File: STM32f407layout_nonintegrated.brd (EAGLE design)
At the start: 61.4 x 71.6 mm, 45 parts, among them Q1 ASF, T3 FDN340P, T4 AP1117_LIN_REG

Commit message: Fixed some wrong info
fixed some stuff
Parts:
- R11, R12, R13, R14: value 83 -> 200
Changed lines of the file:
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@@
 <element name="R1" library="SparkFun-Passives" package="0603-RES" value="10k" x="30.24184375" y="42.22893125" rot="R270"/>
 <element name="R10" library="SparkFun-Passives" package="0603-RES" value="4.7K" x="63.43028125" y="24.979421875" rot="MR180"/>
-<element name="R11" library="SparkFun-Passives" package="0603-RES" value="83" x="28.542509375" y="66.211884375"/>
-<element name="R12" library="SparkFun-Passives" package="0603-RES" value="83" x="28.55059375" y="64.156609375"/>
-<element name="R13" library="SparkFun-Passives" package="0603-RES" value="83" x="28.552184375" y="62.11506875"/>
-<element name="R14" library="SparkFun-Passives" package="0603-RES" value="83" x="28.53085" y="60.0696"/>
+<element name="R11" library="SparkFun-Passives" package="0603-RES" value="200" x="28.542509375" y="66.211884375"/>
+<element name="R12" library="SparkFun-Passives" package="0603-RES" value="200" x="28.55059375" y="64.156609375"/>
+<element name="R13" library="SparkFun-Passives" package="0603-RES" value="200" x="28.552184375" y="62.11506875"/>
+<element name="R14" library="SparkFun-Passives" package="0603-RES" value="200" x="28.53085" y="60.0696"/>
 <element name="R2" library="SparkFun-Passives" package="0603-RES" value="10k" x="30.16184375" y="51.705484375" rot="R90"/>
 <element name="R3" library="SparkFun-Passives" package="0603-RES" value="4.7K" x="35.827084375" y="17.299571875" rot="MR180"/>

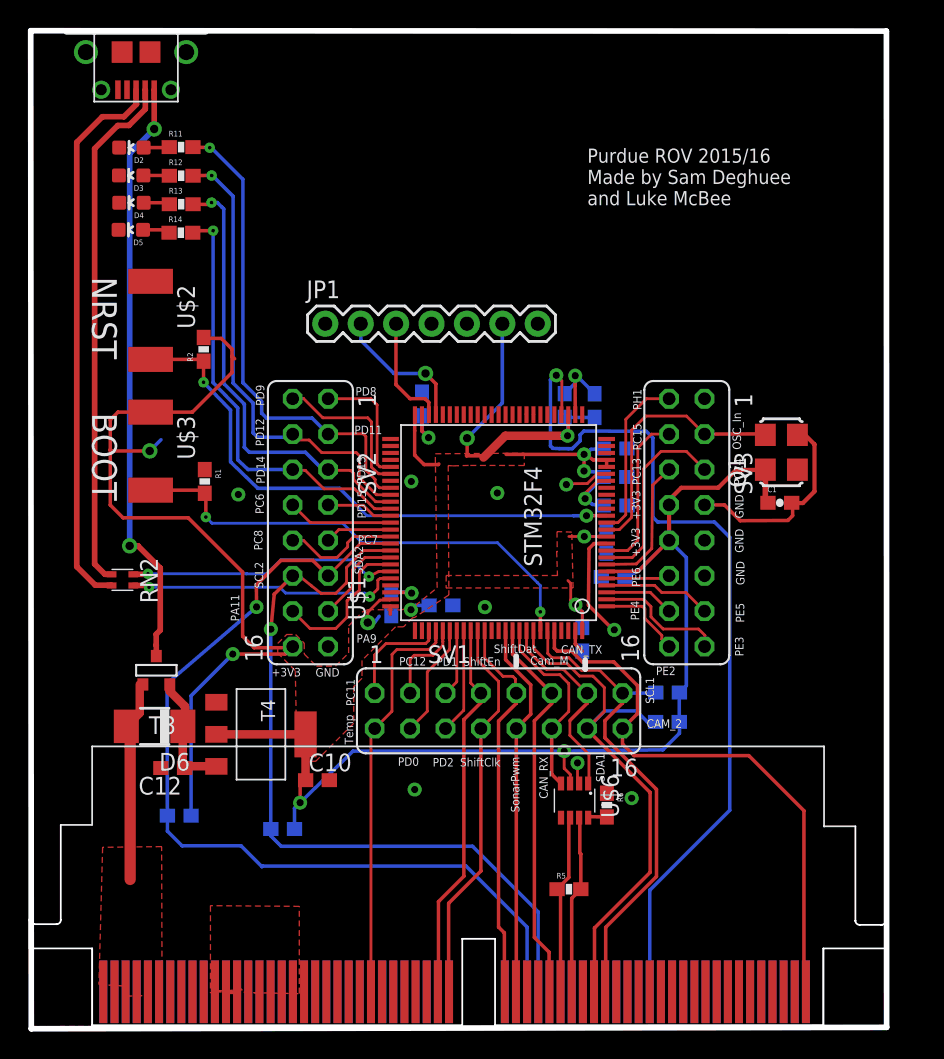
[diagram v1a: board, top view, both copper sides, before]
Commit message: Revision 2.0
Moved LED array, fixed pinout problems
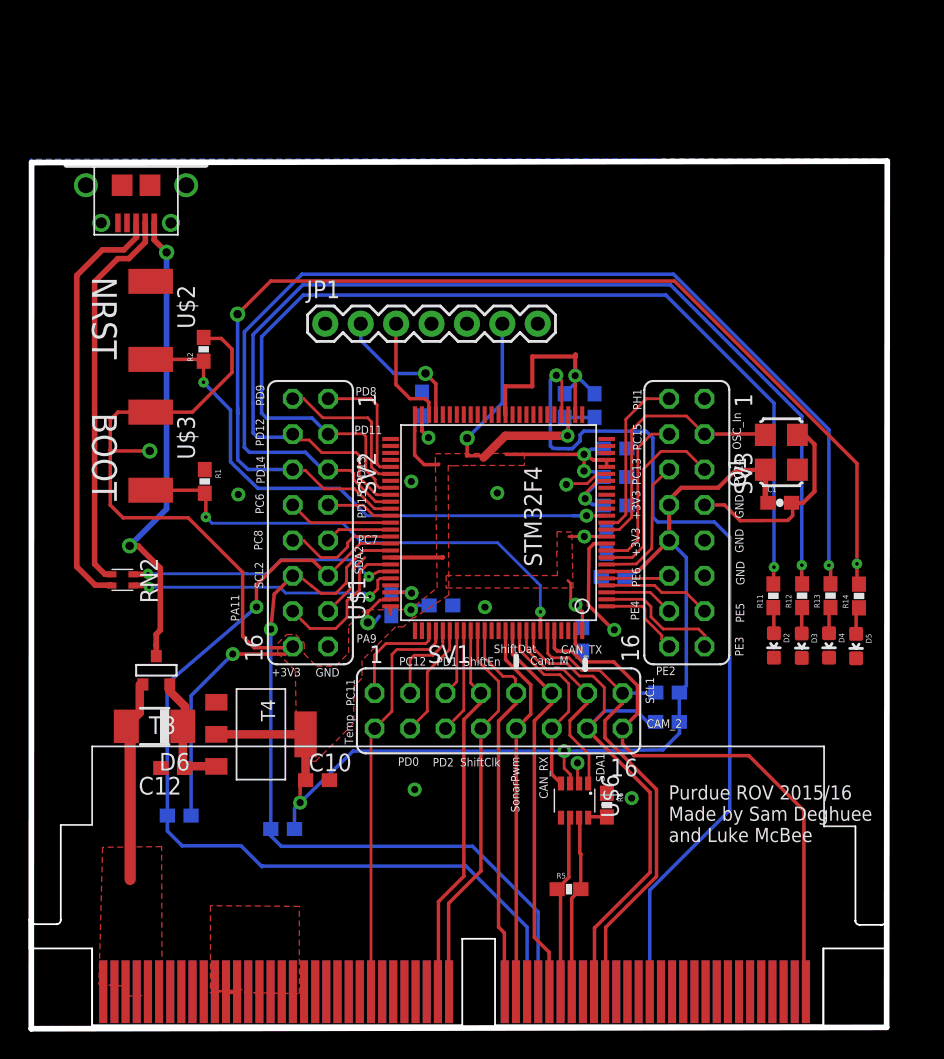
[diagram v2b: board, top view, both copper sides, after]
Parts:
- moved D5 60.0 mm to (77.0, 30.4), turned to 180 degrees
- moved D4 59.3 mm to (75.0, 30.5), turned to 180 degrees
- moved D3 58.7 mm to (73.1, 30.4), turned to 180 degrees
- moved D2 58.3 mm to (71.1, 30.5), turned to 180 degrees
- moved R14 55.2 mm to (77.2, 34.0), turned to 90 degrees
- moved R13 54.4 mm to (75.1, 34.0), turned to 90 degrees
- moved R12 53.8 mm to (73.1, 34.0), turned to 90 degrees
- moved R11 53.3 mm to (71.0, 34.0), turned to 90 degrees
- moved U$5 9.55 mm to (25.3, 64.9)
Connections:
- removed net PB2: U$1.P37
- net +3V3: now also U$1.P68
- net GND: now also U$1.P37
- net PA9: no longer U$1.P68
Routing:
- net PD14: track 31.1 -> 82.8 mm, vias 1 -> 2
- net PD13: track 32.6 -> 80.1 mm
- net PD12: track 33.9 -> 76.7 mm
- net PD11: track 34.9 -> 72.8 mm
- net GND: track 41.6 -> 52.6 mm
- net N$12: track 37.5 -> 28.0 mm
- net N$24: track 40.0 -> 30.4 mm
- net N$57: track 42.7 -> 33.9 mm
- net +3V3: track 203.4 -> 205.7 mm
- net PA9: track 6.79 -> 4.94 mm
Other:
- board size 61.4 x 71.6 mm -> 61.4 x 62.2 mm

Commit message: Fixed PA9 and routed
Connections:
- removed net N$57: T3.1, U$5.P1
- removed net PA9: SV2.13
- new net USBPWR: SV2.13, T3.1, U$1.P68, U$5.P1
- net +3V3: no longer U$1.P68
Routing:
- net USBPWR: track 0.00 -> 58.9 mm, vias 0 -> 3
- net N$57: track 33.9 -> 0.00 mm, vias 2 -> 0
- net PA9: track 4.94 -> 0.00 mm
- net +3V3: track 205.7 -> 202.0 mm
- net I2C3_SDA: track 65.7 -> 66.6 mm, vias 1 -> 3
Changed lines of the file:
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@@
 <wire x1="49.017896875" y1="44.068009375" x2="50.108815625" y2="44.068009375" width="0.254" layer="1"/>
 <wire x1="50.108815625" y1="44.068009375" x2="50.23609375" y2="43.94073125" width="0.254" layer="1"/>
-<contactref element="U$1" pad="P68"/>
-<wire x1="43.56884375" y1="36.773040625" x2="47.318434375" y2="36.773040625" width="0.3048" layer="1"/>
-<wire x1="47.318434375" y1="36.773040625" x2="47.318434375" y2="36.805353125" width="0.3048" layer="1"/>
 </signal>
 <signal name="N$3">
@@
 <contactref element="R3" pad="1"/>
 <contactref element="SV2" pad="12"/>
-<wire x1="43.56884375" y1="37.273040625" x2="41.62684375" y2="37.273040625" width="0.2032" layer="1"/>
-<wire x1="41.62684375" y1="37.273040625" x2="40.41184375" y2="36.058040625" width="0.2032" layer="1"/>
-<wire x1="40.41184375" y1="36.058040625" x2="40.41184375" y2="34.961040625" width="0.2032" layer="1"/>
 <wire x1="40.41184375" y1="34.961040625" x2="40.39584375" y2="34.945040625" width="0.2032" layer="1"/>
 <wire x1="40.39584375" y1="34.945040625" x2="40.38084375" y2="34.945040625" width="0.2032" layer="1"/>
@@
 <wire x1="34.977084375" y1="31.899290625" x2="34.983928125" y2="31.629703125" width="0.254" layer="16"/>
 <via x="34.983928125" y="31.629703125" extent="1-16" drill="0.508"/>
-<wire x1="34.983928125" y1="31.629703125" x2="35.2258375" y2="34.140034375" width="0.254" layer="1"/>
-<wire x1="35.2258375" y1="34.140034375" x2="36.54884375" y2="35.463040625" width="0.254" layer="1"/>
 <wire x1="34.977084375" y1="17.299571875" x2="34.977084375" y2="16.8021875" width="0.254" layer="16"/>
 <wire x1="34.977084375" y1="16.8021875" x2="35.72144375" y2="16.057828125" width="0.254" layer="16"/>
@@
 <wire x1="54.1567125" y1="11.353521875" x2="54.1567125" y2="5.628225" width="0.254" layer="16"/>
 <wire x1="54.1567125" y1="5.628225" x2="54.163659375" y2="5.621278125" width="0.254" layer="16"/>
+<wire x1="40.41184375" y1="34.961040625" x2="40.41184375" y2="36.22315" width="0.2032" layer="1"/>
+<wire x1="40.41184375" y1="36.22315" x2="41.456471875" y2="37.267778125" width="0.2032" layer="1"/>
+<wire x1="41.456471875" y1="37.267778125" x2="43.56358125" y2="37.267778125" width="0.2032" layer="1"/>
+<wire x1="43.56358125" y1="37.267778125" x2="43.56884375" y2="37.273040625" width="0.2032" layer="1"/>
+<wire x1="36.54884375" y1="35.463040625" x2="34.983928125" y2="33.898125" width="0.2032" layer="1"/>
+<wire x1="34.983928125" y1="33.898125" x2="34.983928125" y2="31.629703125" width="0.2032" layer="1"/>
 </signal>
 <signal name="I2C3_SDA">
@@
 <wire x1="41.39884375" y1="37.773040625" x2="39.08884375" y2="35.463040625" width="0.2032" layer="1"/>
 <wire x1="27.561375" y1="18.2559375" x2="27.539353125" y2="27.739171875" width="0.254" layer="16"/>
-<wire x1="27.539353125" y1="27.739171875" x2="33.954415625" y2="33.223175" width="0.254" layer="16"/>
 <via x="33.954415625" y="33.223175" extent="1-16" drill="0.508"/>
 <wire x1="33.954415625" y1="33.223175" x2="33.94585625" y2="34.804046875" width="0.254" layer="1"/>
@@
 <wire x1="48.98438125" y1="14.63629375" x2="34.38481875" y2="14.63629375" width="0.254" layer="16"/>
 <wire x1="34.38481875" y1="14.63629375" x2="34.343415625" y2="14.594890625" width="0.254" layer="16"/>
+<via x="31.108665625" y="31.83608125" extent="1-16" drill="0.6"/>
+<wire x1="31.108665625" y1="31.83608125" x2="29.4826375" y2="29.419990625" width="0.2032" layer="1"/>
+<wire x1="29.4826375" y1="29.419990625" x2="29.4826375" y2="28.851025" width="0.2032" layer="1"/>
+<via x="29.4826375" y="28.851025" extent="1-16" drill="0.6"/>
+<wire x1="29.4826375" y1="28.851025" x2="28.65120625" y2="28.851025" width="0.2032" layer="16"/>
+<wire x1="28.65120625" y1="28.851025" x2="27.539353125" y2="27.739171875" width="0.2032" layer="16"/>
+<wire x1="33.954415625" y1="33.223175" x2="32.567321875" y2="31.83608125" width="0.2032" layer="16"/>
+<wire x1="32.567321875" y1="31.83608125" x2="31.108665625" y2="31.83608125" width="0.2032" layer="16"/>
 </signal>
 <signal name="+5V">
@@
 <via x="42.0186875" y="35.404221875" extent="1-16" drill="0.254"/>
 <wire x1="33.2607875" y1="35.60138125" x2="34.681846875" y2="35.60138125" width="0.2032" layer="16"/>
-<wire x1="34.681846875" y1="35.60138125" x2="35.694721875" y2="36.605209375" width="0.2032" layer="16"/>
-<wire x1="35.694721875" y1="36.605209375" x2="40.788484375" y2="36.605209375" width="0.2032" layer="16"/>
+<wire x1="34.681846875" y1="35.60138125" x2="35.671021875" y2="36.689859375" width="0.2032" layer="16"/>
+<wire x1="35.671021875" y1="36.689859375" x2="40.764784375" y2="36.689859375" width="0.2032" layer="16"/>
 <wire x1="43.56884375" y1="35.773040625" x2="42.732465625" y2="35.773040625" width="0.2032" layer="1"/>
 <wire x1="42.732465625" y1="35.773040625" x2="42.0186875" y2="35.404221875" width="0.2032" layer="1"/>
 <wire x1="42.0186875" y1="35.404221875" x2="41.9281875" y2="35.41701875" width="0.2032" layer="16"/>
-<wire x1="41.9281875" y1="35.41701875" x2="40.788484375" y2="36.605209375" width="0.2032" layer="16"/>
+<wire x1="41.9281875" y1="35.41701875" x2="40.764784375" y2="36.689859375" width="0.2032" layer="16"/>
 <wire x1="25.11045625" y1="35.5667" x2="26.166109375" y2="35.5667" width="0.4064" layer="1"/>
 <wire x1="26.166109375" y1="35.5667" x2="26.166109375" y2="35.60463125" width="0.4064" layer="1"/>
@@
 <wire x1="21.059978125" y1="57.00636875" x2="21.059978125" y2="36.113871875" width="0.4064" layer="1"/>
 </signal>
-<signal name="N$57">
+<signal name="USBPWR">
 <contactref element="U$5" pad="P1"/>
 <contactref element="T3" pad="1"/>
@@
 <wire x1="27.504975" y1="58.66146875" x2="27.504975" y2="40.258465625" width="0.4064" layer="16"/>
 <wire x1="27.504975" y1="40.258465625" x2="24.8554" y2="37.608890625" width="0.4064" layer="16"/>
+<contactref element="U$1" pad="P68"/>
+<wire x1="27.049146875" y1="36.011384375" x2="27.049146875" y2="31.846184375" width="0.2032" layer="1"/>
+<wire x1="27.049146875" y1="31.846184375" x2="27.075425" y2="31.81990625" width="0.2032" layer="1"/>
+<wire x1="43.56884375" y1="36.773040625" x2="43.602453125" y2="36.73943125" width="0.2032" layer="1" curve="90"/>
+<contactref element="SV2" pad="13"/>
+<wire x1="39.08884375" y1="32.923040625" x2="39.111925" y2="32.923040625" width="0.2032" layer="1"/>
+<wire x1="39.111925" y1="32.923040625" x2="40.897528125" y2="34.70864375" width="0.2032" layer="1"/>
+<wire x1="40.897528125" y1="34.70864375" x2="40.897528125" y2="36.139609375" width="0.2032" layer="1"/>
+<wire x1="40.897528125" y1="36.139609375" x2="41.49735" y2="36.73943125" width="0.2032" layer="1"/>
+<wire x1="41.49735" y1="36.73943125" x2="43.535234375" y2="36.73943125" width="0.2032" layer="1"/>
+<wire x1="43.535234375" y1="36.73943125" x2="43.56884375" y2="36.773040625" width="0.2032" layer="1"/>
+<wire x1="39.08884375" y1="32.923040625" x2="37.87411875" y2="31.708315625" width="0.2032" layer="16"/>
+<wire x1="37.87411875" y1="31.708315625" x2="35.955671875" y2="31.708315625" width="0.2032" layer="16"/>
+<wire x1="35.955671875" y1="31.708315625" x2="35.2856" y2="32.3783875" width="0.2032" layer="16"/>
+<wire x1="35.2856" y1="32.3783875" x2="34.160415625" y2="32.3783875" width="0.2032" layer="16"/>
+<wire x1="34.160415625" y1="32.3783875" x2="32.35635" y2="30.7323375" width="0.2032" layer="16"/>
+<wire x1="32.35635" y1="30.7323375" x2="28.552928125" y2="30.7323375" width="0.2032" layer="16"/>
+<via x="28.552928125" y="30.7323375" extent="1-16" drill="0.6"/>
+<wire x1="28.552928125" y1="30.7323375" x2="27.604540625" y2="31.557825" width="0.2032" layer="1"/>
+<wire x1="27.604540625" y1="31.557825" x2="27.049146875" y2="31.557825" width="0.2032" layer="1"/>
 </signal>
 <signal name="N$58">
@@
 <wire x1="36.56384375" y1="48.178040625" x2="36.54884375" y2="48.163040625" width="0.2032" layer="1"/>
 </signal>
-<signal name="PA9">
-<contactref element="SV2" pad="13"/>
-<wire x1="41.72284375" y1="36.773040625" x2="40.82984375" y2="35.880040625" width="0.2032" layer="1"/>
-<wire x1="40.82984375" y1="35.880040625" x2="40.82984375" y2="34.664040625" width="0.2032" layer="1"/>
-<wire x1="40.82984375" y1="34.664040625" x2="39.08884375" y2="32.923040625" width="0.2032" layer="1"/>
-</signal>
 <signal name="PC7">

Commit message: Better Routing
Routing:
- net USBPWR: track 58.9 -> 73.6 mm, vias 3 -> 2
- net GND: track 52.6 -> 43.7 mm
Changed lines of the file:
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@@
 <contactref element="JP1" pad="5"/>
 <contactref element="U$1" pad="P37"/>
-<wire x1="51.81884375" y1="47.023040625" x2="51.788096875" y2="47.023040625" width="0.3048" layer="1"/>
-<wire x1="51.788096875" y1="47.023040625" x2="51.788096875" y2="49.05165625" width="0.3048" layer="1"/>
-<wire x1="51.788096875" y1="49.05165625" x2="53.7391625" y2="49.05165625" width="0.3048" layer="1"/>
-<wire x1="53.7391625" y1="49.05165625" x2="53.7391625" y2="51.193559375" width="0.3048" layer="1"/>
-<wire x1="53.7391625" y1="51.193559375" x2="56.856628125" y2="51.193559375" width="0.3048" layer="1"/>
-<wire x1="56.856628125" y1="51.193559375" x2="56.856628125" y2="51.3208" width="0.3048" layer="1"/>
-<wire x1="56.856628125" y1="51.3208" x2="56.815253125" y2="51.3208" width="0.3048" layer="1"/>
-<wire x1="56.815253125" y1="51.3208" x2="56.815253125" y2="49.814884375" width="0.3048" layer="1"/>
+<wire x1="51.81884375" y1="47.023040625" x2="51.827284375" y2="47.0254875" width="0.3048" layer="1"/>
+<wire x1="51.827284375" y1="47.0254875" x2="51.788096875" y2="49.05165625" width="0.3048" layer="1"/>
 </signal>
 <signal name="+3V3">
@@
 <contactref element="SV2" pad="13"/>
 <wire x1="39.08884375" y1="32.923040625" x2="39.111925" y2="32.923040625" width="0.2032" layer="1"/>
-<wire x1="39.111925" y1="32.923040625" x2="40.897528125" y2="34.70864375" width="0.2032" layer="1"/>
-<wire x1="40.897528125" y1="34.70864375" x2="40.897528125" y2="36.139609375" width="0.2032" layer="1"/>
-<wire x1="40.897528125" y1="36.139609375" x2="41.49735" y2="36.73943125" width="0.2032" layer="1"/>
-<wire x1="41.49735" y1="36.73943125" x2="43.535234375" y2="36.73943125" width="0.2032" layer="1"/>
-<wire x1="43.535234375" y1="36.73943125" x2="43.56884375" y2="36.773040625" width="0.2032" layer="1"/>
-<wire x1="39.08884375" y1="32.923040625" x2="37.87411875" y2="31.708315625" width="0.2032" layer="16"/>
-<wire x1="37.87411875" y1="31.708315625" x2="35.955671875" y2="31.708315625" width="0.2032" layer="16"/>
-<wire x1="35.955671875" y1="31.708315625" x2="35.2856" y2="32.3783875" width="0.2032" layer="16"/>
-<wire x1="35.2856" y1="32.3783875" x2="34.160415625" y2="32.3783875" width="0.2032" layer="16"/>
-<wire x1="34.160415625" y1="32.3783875" x2="32.35635" y2="30.7323375" width="0.2032" layer="16"/>
-<wire x1="32.35635" y1="30.7323375" x2="28.552928125" y2="30.7323375" width="0.2032" layer="16"/>
-<via x="28.552928125" y="30.7323375" extent="1-16" drill="0.6"/>
-<wire x1="28.552928125" y1="30.7323375" x2="27.604540625" y2="31.557825" width="0.2032" layer="1"/>
-<wire x1="27.604540625" y1="31.557825" x2="27.049146875" y2="31.557825" width="0.2032" layer="1"/>
+<wire x1="43.556103125" y1="36.7603" x2="43.56884375" y2="36.773040625" width="0.2032" layer="1"/>
+<wire x1="43.535234375" y1="36.73943125" x2="43.556103125" y2="36.7603" width="0.2032" layer="1"/>
+<wire x1="43.556103125" y1="36.7603" x2="45.0873625" y2="36.7603" width="0.2032" layer="1"/>
+<wire x1="45.0873625" y1="36.7603" x2="46.114559375" y2="37.787496875" width="0.2032" layer="1"/>
+<wire x1="46.114559375" y1="37.787496875" x2="46.114559375" y2="42.61243125" width="0.2032" layer="1"/>
+<wire x1="46.114559375" y1="42.61243125" x2="44.69396875" y2="44.033021875" width="0.2032" layer="1"/>
+<wire x1="44.69396875" y1="44.033021875" x2="44.69396875" y2="46.87921875" width="0.2032" layer="1"/>
+<wire x1="44.69396875" y1="46.87921875" x2="39.9077" y2="51.6654875" width="0.2032" layer="1"/>
+<wire x1="39.9077" y1="51.6654875" x2="33.504075" y2="51.6654875" width="0.2032" layer="1"/>
+<wire x1="33.504075" y1="51.6654875" x2="31.5371125" y2="53.63245" width="0.2032" layer="1"/>
+<wire x1="31.5371125" y1="53.63245" x2="31.5371125" y2="54.62933125" width="0.2032" layer="1"/>
+<wire x1="31.5371125" y1="54.62933125" x2="27.504975" y2="58.66146875" width="0.2032" layer="1"/>
+<wire x1="43.535234375" y1="36.73943125" x2="39.08884375" y2="32.923040625" width="0" layer="19" extent="1-1"/>
 </signal>
 <signal name="N$58">
